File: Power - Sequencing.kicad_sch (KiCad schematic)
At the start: 0 parts

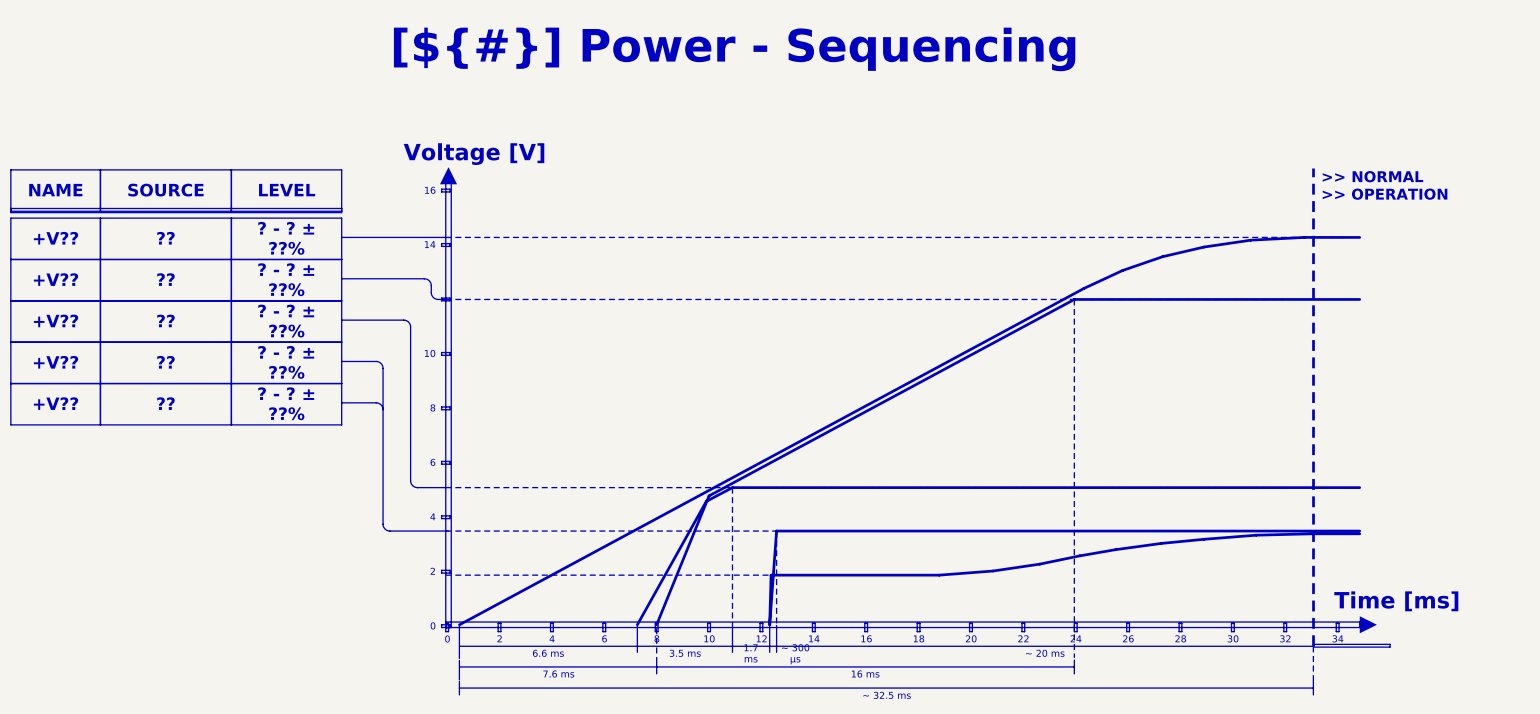
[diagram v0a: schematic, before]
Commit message: feat: Changed templates to be specific to Ryan Dynamics
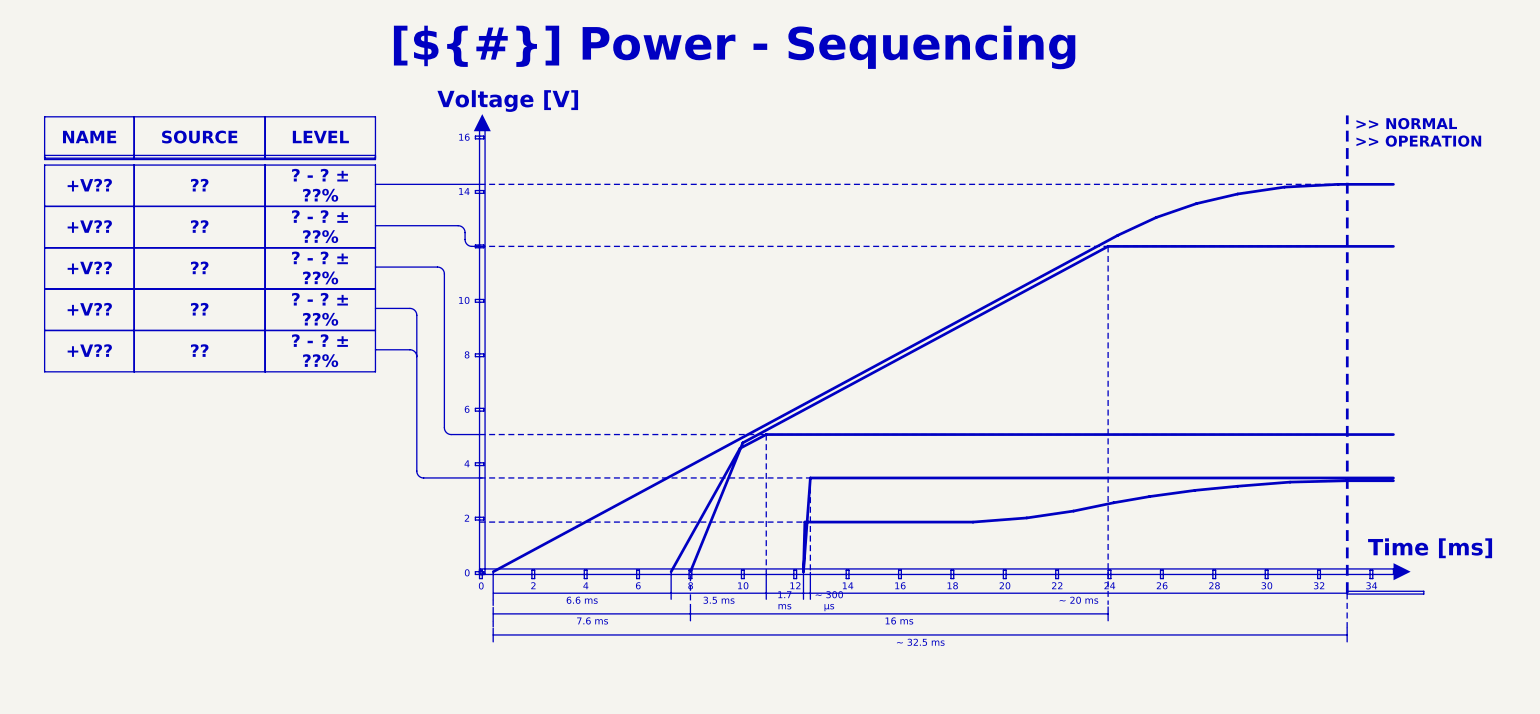
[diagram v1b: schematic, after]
